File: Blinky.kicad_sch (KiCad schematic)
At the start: 46 parts, among them J1 DTF13-4P-G003, J25 Conn_01x01, J26 Conn_01x01, J27 Conn_01x01, J28 Conn_01x01, J29 Conn_01x01, J30 Conn_01x01, J5 1053091102, Q1 IPD90P03P404ATMA2, Q2 IPD90P03P404ATMA2, U1 DCM4623TD2J13D0T70, U2 LTC3638xMSE, U3 DCM4623TD2J13D0T70

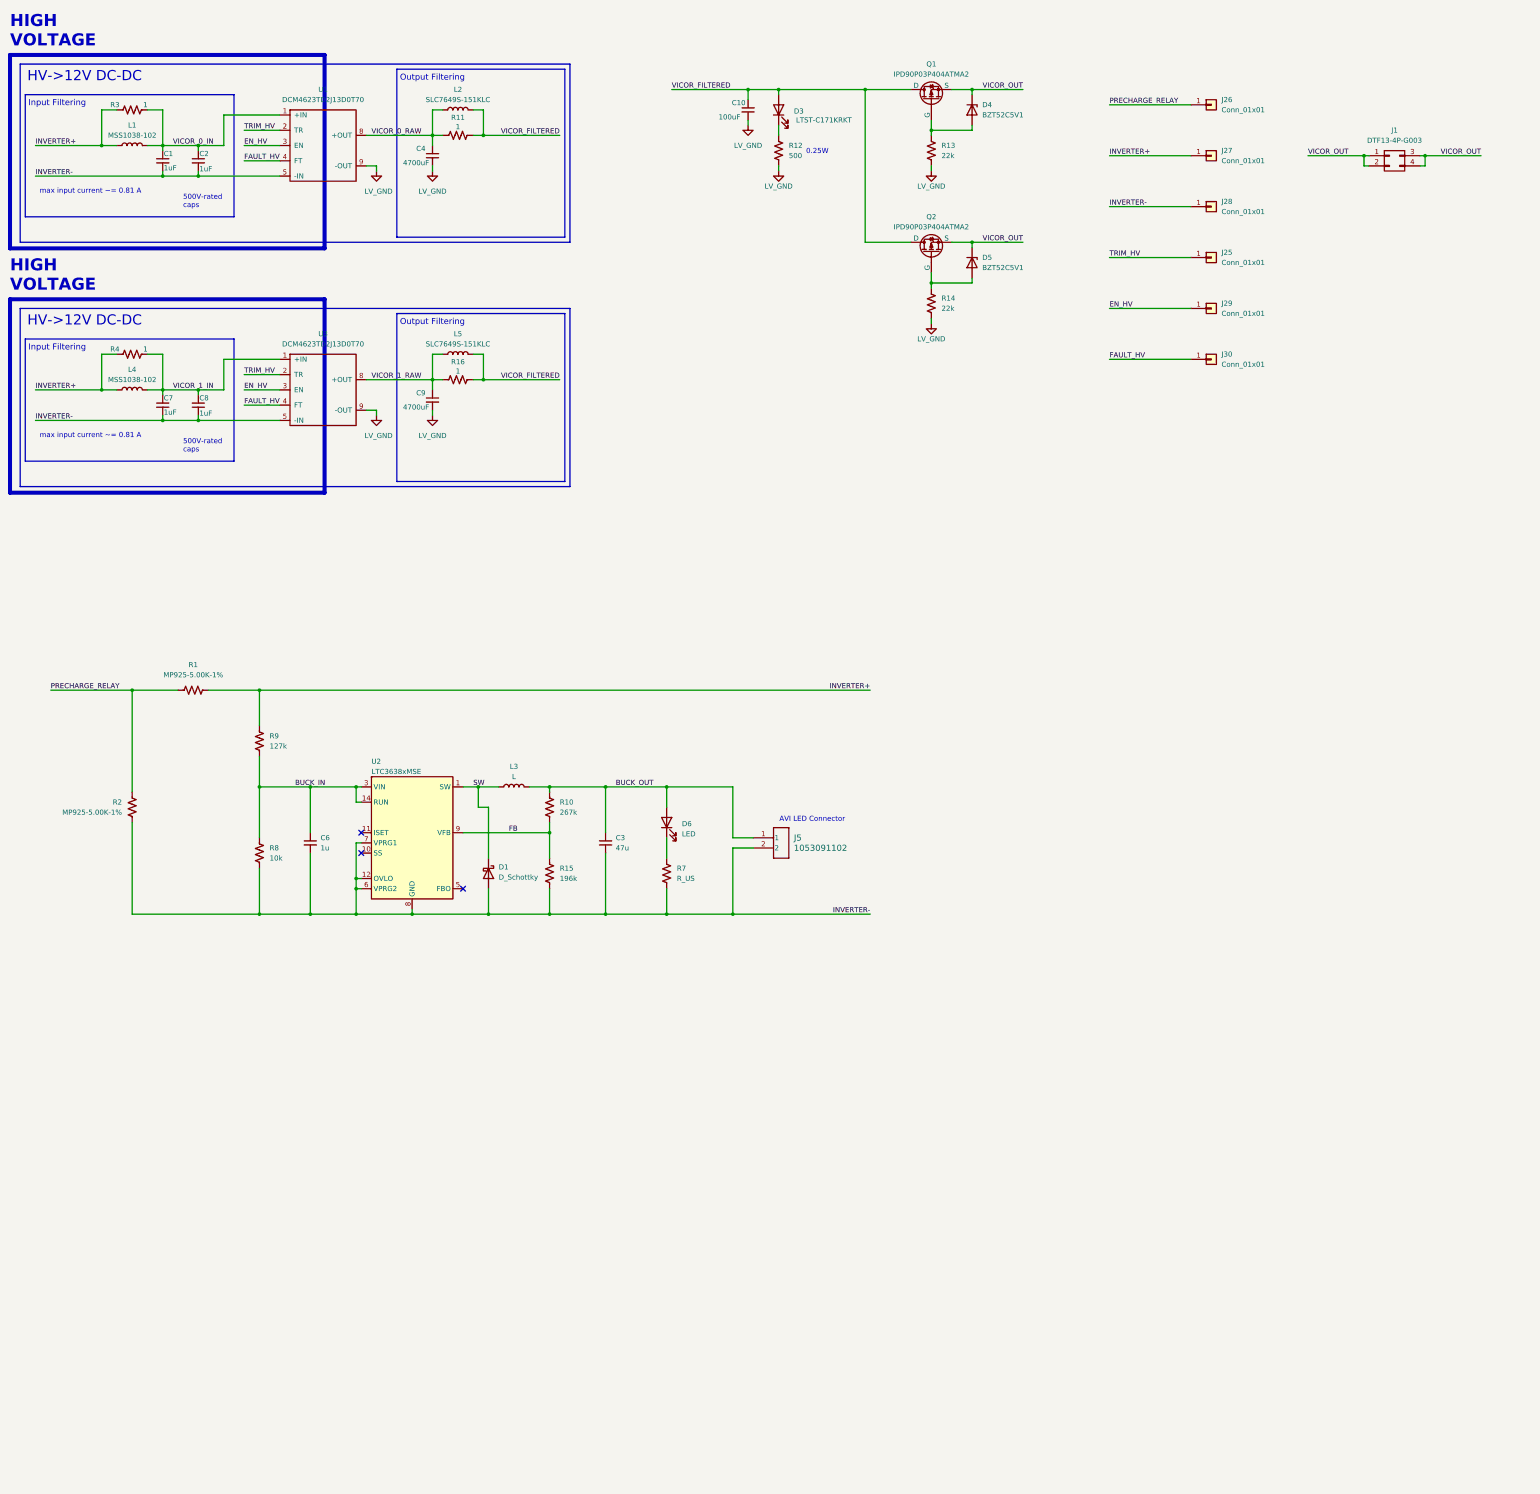
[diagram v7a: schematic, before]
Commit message: turning blinky into a DC-DC converter board
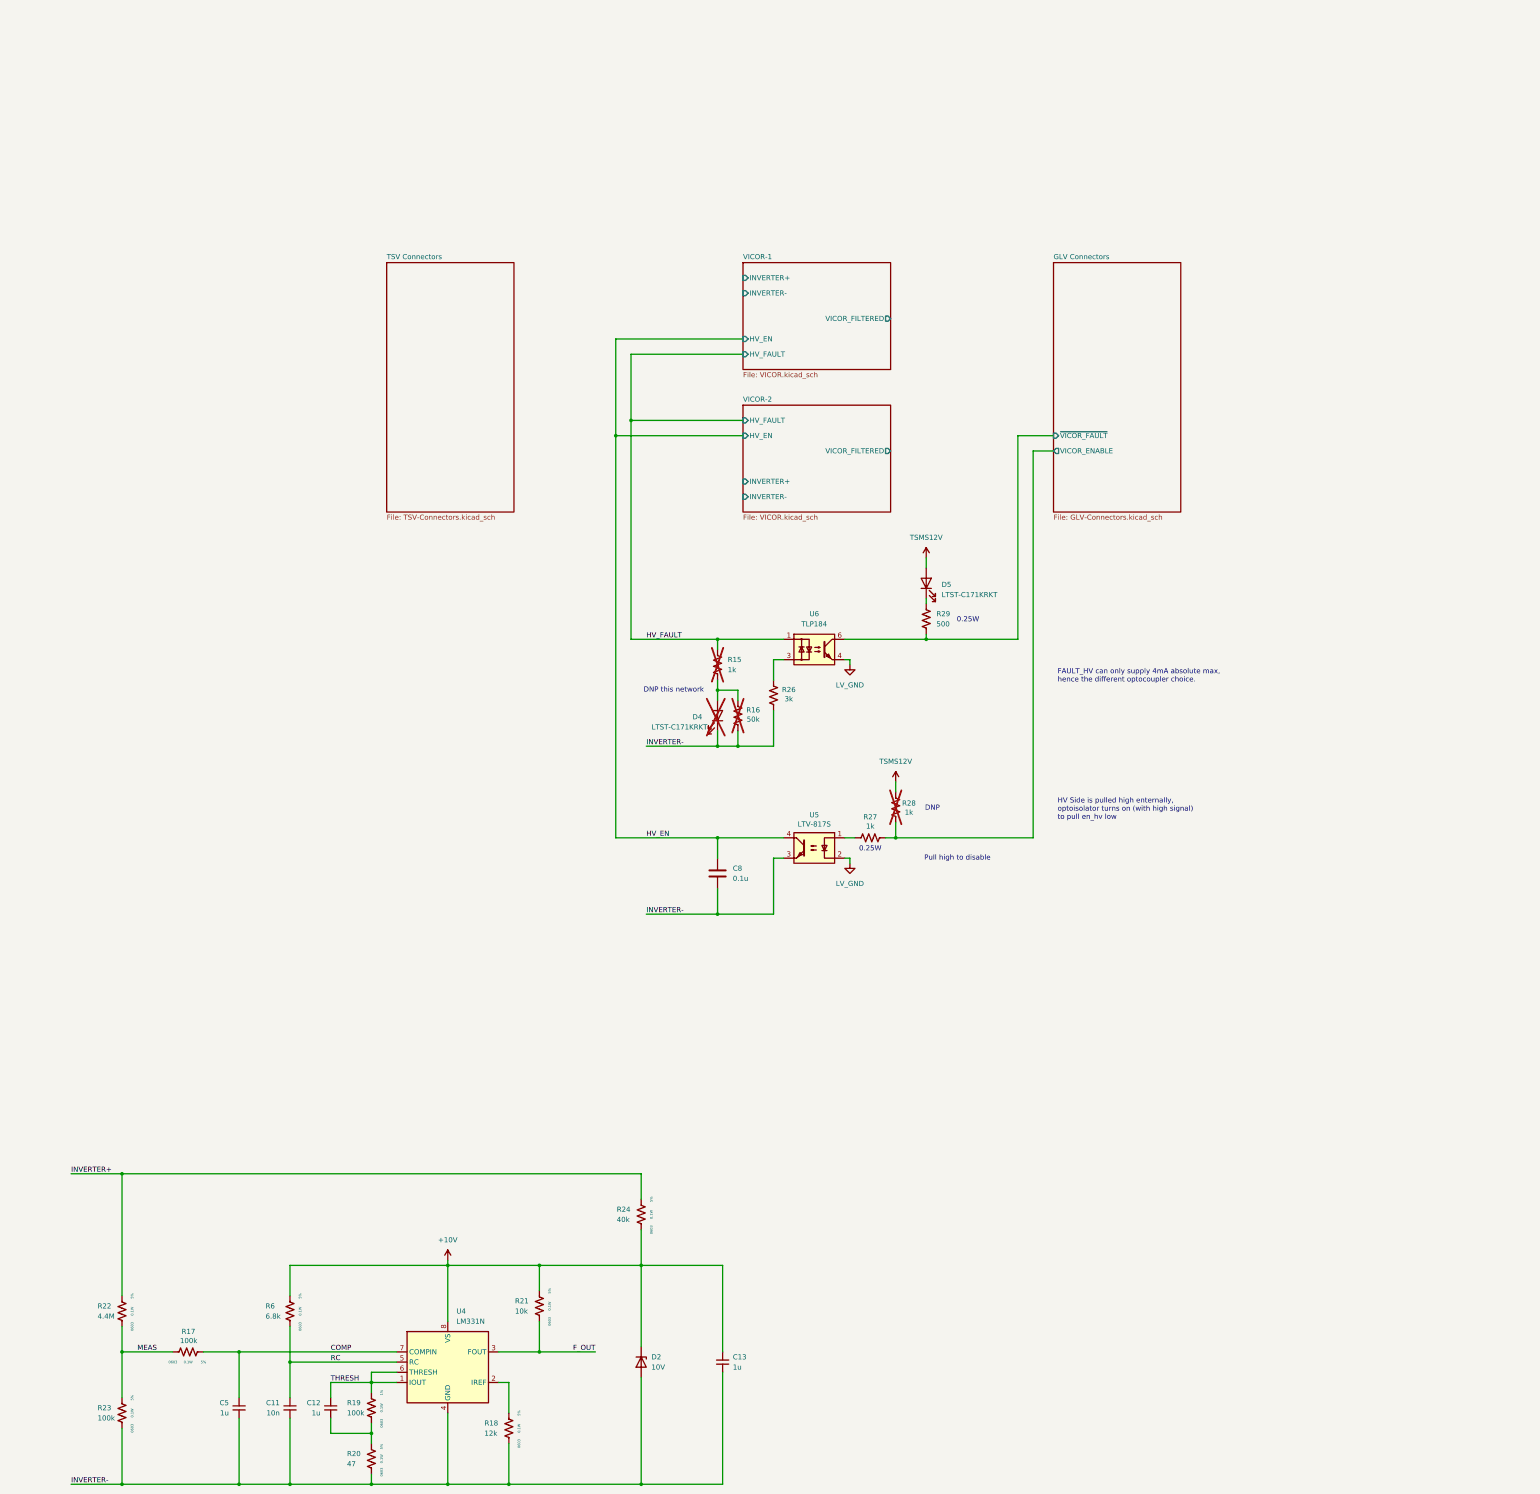
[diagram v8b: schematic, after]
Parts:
- removed C1, C2, C7, C8: 1uF, Capacitor_THT:C_Rect_L18.0mm_W8.0mm_P15.00mm_FKS3_FKP3, symbol Device:C_Small
- removed C10: 100uF, Capacitor_THT:C_Radial_D12.5mm_H25.0mm_P5.00mm, symbol Device:C_Small
- removed C3: 47u, Capacitor_SMD:C_0603_1608Metric_Pad1.08x0.95mm_HandSolder, symbol Device:C_Small
- removed C4, C9: 4700uF, Capacitor_THT:C_Radial_D12.5mm_H25.0mm_P5.00mm, symbol Device:C_Small
- removed C6: 1u, Capacitor_SMD:C_0603_1608Metric_Pad1.08x0.95mm_HandSolder, symbol Device:C_Small
- removed D1: D_Schottky, symbol Device:D_Schottky
- removed D3: LTST-C171KRKT, LED_SMD:LED_0805_2012Metric, symbol Device:LED
- removed D4, D5: BZT52C5V1, Diode_SMD:D_SOD-123, symbol Device:D_Zener
- removed D6: LED, LED_SMD:LED_0805_2012Metric_Pad1.15x1.40mm_HandSolder, symbol Device:LED
- removed J1: DTF13-4P-G003, AERO_Connectors:DTF13-4P-G003, symbol AERO_Connectors:DTF13-4P-G003
- removed J25, J26, J27, J28, J29, J30: Conn_01x01, Connector_Hirose:Hirose_DF63M-1P-3.96DSA_1x01_P3.96mm_Vertical, symbol Connector_Generic:Conn_01x01
- removed J5: 1053091102, AERO_Connectors:1053091102, symbol AERO_Connectors:1053091102
- removed L1, L4: MSS1038-102, AERO_Inductors:MSS1038-102, symbol AERO_Inductors:MSS1038-102
- removed L2, L5: SLC7649S-151KLC, AERO_Inductors:SLC7649S-151KLC, symbol AERO_Inductors:SLC7649S-151KLC
- removed L3: L, symbol Device:L
- removed Q1, Q2: IPD90P03P404ATMA2, AERO_Transistors:IPD90P03P404ATMA2, symbol AERO_Transistors:IPD90P03P404ATMA2
- removed R1, R2: MP925-5.00K-1%, AERO_Resistors:MP925-5.00K-1%_TabUp, symbol AERO_Resistors:MP925-5.00K-1%
- removed R10: 267k, Resistor_SMD:R_1206_3216Metric_Pad1.30x1.75mm_HandSolder, symbol Device:R_US
- removed R11, R3, R4: 1, Resistor_SMD:R_2512_6332Metric_Pad1.40x3.35mm_HandSolder, symbol Device:R_US
- removed R12: 500, Resistor_SMD:R_0805_2012Metric_Pad1.20x1.40mm_HandSolder, symbol Device:R_US
- removed R13, R14: 22k, Resistor_SMD:R_0603_1608Metric_Pad0.98x0.95mm_HandSolder, symbol Device:R_US
- removed R7: R_US, Resistor_SMD:R_1206_3216Metric_Pad1.30x1.75mm_HandSolder, symbol Device:R_US
- removed R8: 10k, Resistor_SMD:R_1206_3216Metric_Pad1.30x1.75mm_HandSolder, symbol Device:R_US
- removed R9: 127k, Resistor_SMD:R_1206_3216Metric_Pad1.30x1.75mm_HandSolder, symbol Device:R_US
- removed U1, U3: DCM4623TD2J13D0T70, AERO_Regulators:DCM4623TD2J13D0T70, symbol AERO_Regulators:DCM4623TD2J13D0T70
- removed U2: LTC3638xMSE, Package_SO:Analog_MSOP-12-16-1EP_3x4.039mm_P0.5mm_EP1.651x2.845mm, symbol AERO_Regulators:LTC3638xMSE
- added C11: 10n, symbol Device:C_Small
- added C12, C13, C5: 1u, symbol Device:C_Small
- added C8: 0.1u, Capacitor_SMD:C_0603_1608Metric, symbol Device:C
- added D2: 10V, symbol Device:D_Zener
- added D4, D5: LTST-C171KRKT, LED_SMD:LED_0805_2012Metric, symbol Device:LED
- added R17, R19, R23: 100k, Resistor_SMD:R_0603_1608Metric_Pad0.98x0.95mm_HandSolder, symbol AERO_Resistors:R_0603
- added R18: 12k, Resistor_SMD:R_0603_1608Metric_Pad0.98x0.95mm_HandSolder, symbol AERO_Resistors:R_0603
- added R20: 47, Resistor_SMD:R_0603_1608Metric_Pad0.98x0.95mm_HandSolder, symbol AERO_Resistors:R_0603
- added R21: 10k, Resistor_SMD:R_0603_1608Metric_Pad0.98x0.95mm_HandSolder, symbol AERO_Resistors:R_0603
- added R22: 4.4M, Resistor_SMD:R_0603_1608Metric_Pad0.98x0.95mm_HandSolder, symbol AERO_Resistors:R_0603
- added R24: 40k, Resistor_SMD:R_0603_1608Metric_Pad0.98x0.95mm_HandSolder, symbol AERO_Resistors:R_0603
- added R26: 3k, Resistor_SMD:R_0603_1608Metric_Pad0.98x0.95mm_HandSolder, symbol Device:R_US
- added R27: 1k, Resistor_SMD:R_0805_2012Metric_Pad1.20x1.40mm_HandSolder, symbol Device:R_US
- added R28: 1k, Resistor_SMD:R_0603_1608Metric_Pad0.98x0.95mm_HandSolder, symbol Device:R_US
- added R29: 500, Resistor_SMD:R_0805_2012Metric_Pad1.20x1.40mm_HandSolder, symbol Device:R_US
- added R6: 6.8k, Resistor_SMD:R_0603_1608Metric_Pad0.98x0.95mm_HandSolder, symbol AERO_Resistors:R_0603
- added U4: LM331N, Package_DIP:DIP-8_W7.62mm, symbol Analog:LM331N
- added U5: LTV-817S, Package_DIP:SMDIP-4_W9.53mm, symbol Isolator:LTV-817S
- added U6: TLP184, Package_SO:Toshiba_SOIC-4-6_4.4x3.6mm_P1.27mm, symbol Isolator:TLP184
- R15: value 196k -> 1k; footprint Resistor_SMD:R_1206_3216Metric_Pad1.30x1.75mm_HandSolder -> Resistor_SMD:R_0603_1608Metric_Pad0.98x0.95mm_HandSolder; now not fitted
- R16: value 1 -> 50k; footprint Resistor_SMD:R_2512_6332Metric_Pad1.40x3.35mm_HandSolder -> Resistor_SMD:R_0603_1608Metric_Pad0.98x0.95mm_HandSolder; Digikey part number 2019-RK73H1JTTD1002FCT-ND -> RMCF0603FT1K00CT-ND; Manufacturer_Part_Number RK73H1JTTD1002F -> RMCF0603FT1K00; now not fitted
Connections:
- net VICOR_FILTERED is gone; now on net INVERTER-: R16.1
- net INVERTER+: now also R22.2, R24.2
- net INVERTER-: now also C11.2, C13.2, C5.2, C8.2, D2.2 (A), D4.1 (K), R18.1, R20.1, R23.1, R26.1, U4.4 (GND), U5.3; no longer R15.2
- net LV_GND: now also U5.2, U6.4
- net FB renamed HV_FAULT
- net HV_FAULT: now also U6.1
- net VICOR_1_RAW: no longer names the net of R16.2
- net VICOR_1_RAW: now also R15.2, D4.2 (A)
- new net: R18.2, U4.2 (IREF)
- new net: R26.2, U6.3
- new net: D5.1 (K), R29.1
- new net: C12.2, R19.1, R20.2
- new net: R27.2, U5.1
- new net +10V: C13.1, D2.1 (K), R21.2, R24.1, R6.2, U4.8 (VS)
- new net COMP: C5.1, R17.2, U4.7 (COMPIN)
- new net F_OUT: R21.1, U4.3 (FOUT)
- new net GLV Connectors/VICOR_ENABLE: R27.1, R28.2
- new net GLV Connectors/~{VICOR_FAULT}: R29.2, U6.6
- new net HV_EN: C8.1, U5.4
- new net MEAS: R17.1, R22.1, R23.2
- new net RC: C11.1, R6.1, U4.5 (RC)
- new net THRESH: C12.1, R19.2, U4.1 (IOUT), U4.6 (THRESH)
- new net TSMS12V: D5.2 (A), R28.1
- no-connect marks 3 -> 0
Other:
- added sheet GLV Connectors (GLV-Connectors.kicad_sch)
- added sheet TSV Connectors (TSV-Connectors.kicad_sch)
- added sheet VICOR-1 (VICOR.kicad_sch)
- added sheet VICOR-2 (VICOR.kicad_sch)
- note added: "DNP"
- note added: "DNP this network"
- note added: "FAULT_HV can only supply 4mA absolute max, hence the different optocoupler choice."
- note added: "HV Side is pulled high enternally, optoisolator turns on (with high signal) to pull en_hv low"
- note added: "Pull high to disable"
- note removed: "500V-rated caps"
- note removed: "AVI LED Connector"
- note removed: "HIGH VOLTAGE"
- note removed: "HV->12V DC-DC"
- note removed: "Input Filtering"
- note removed: "Output Filtering"
- note removed: "max input current ~= 0.81 A"
